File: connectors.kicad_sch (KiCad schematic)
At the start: 2 parts

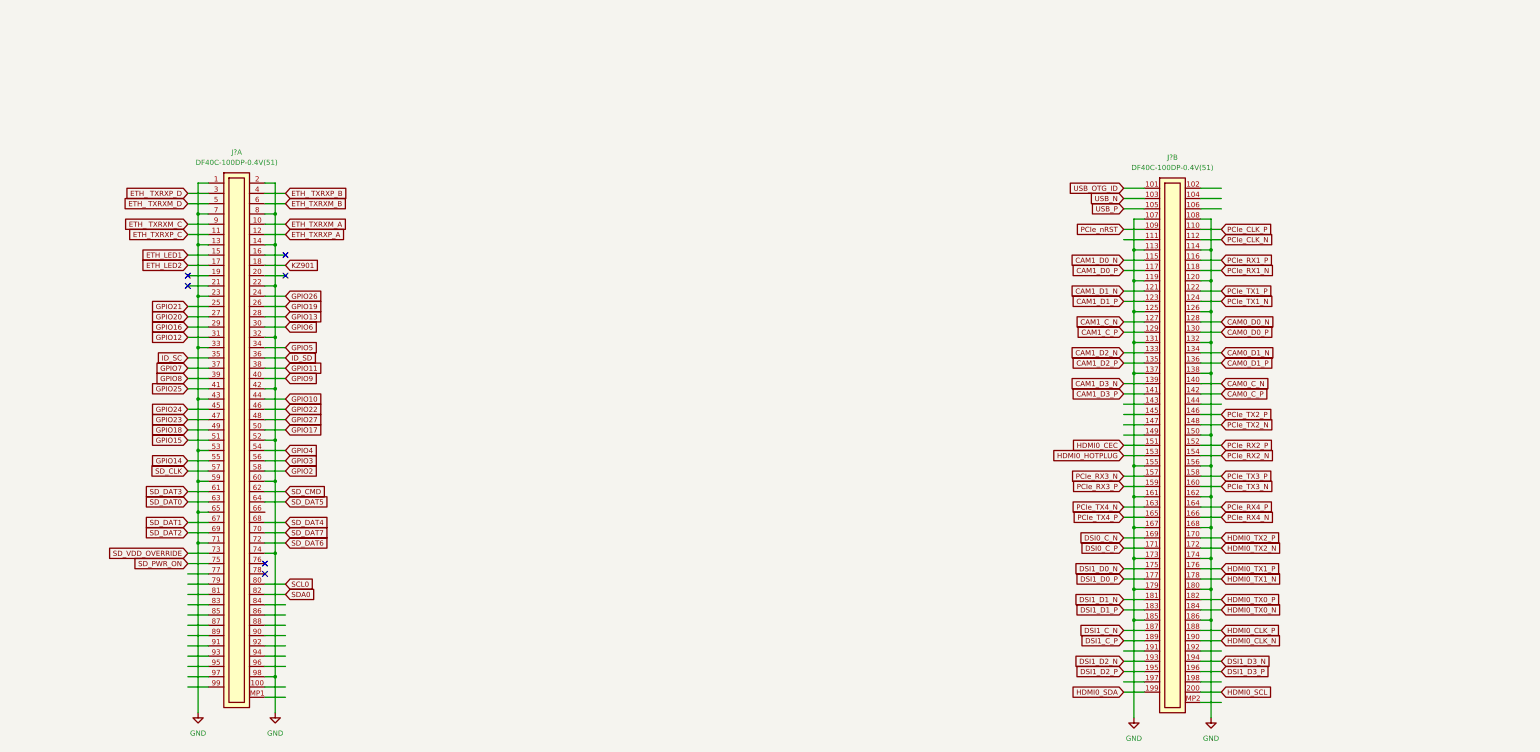
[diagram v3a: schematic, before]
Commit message: [#52579] Connect CSI and DSI to CrossLink
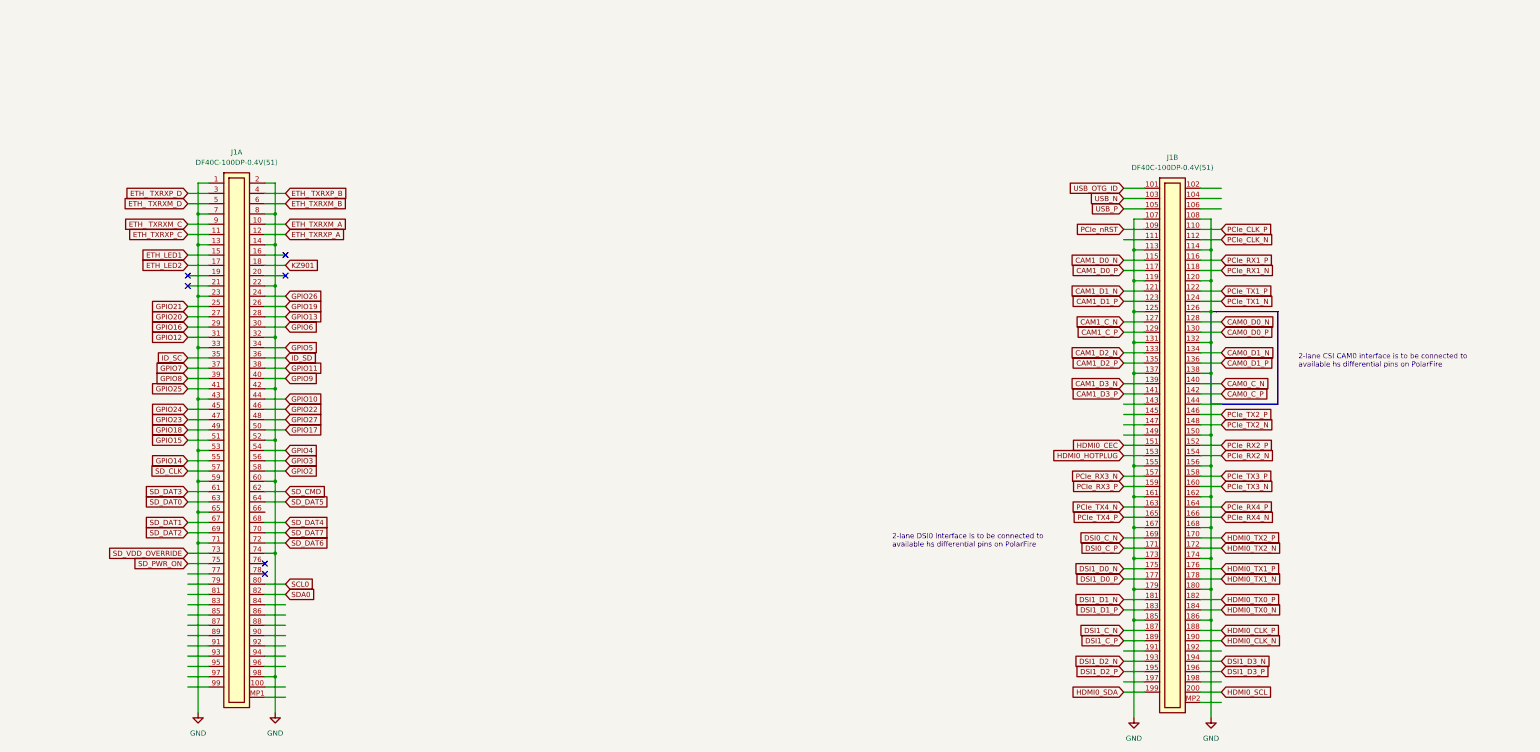
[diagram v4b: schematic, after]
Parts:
- gave numbers to parts that had none: 1
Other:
- note added: "2-lane CSI CAM0 interface is to be connected to available hs differential pins on PolarFire"
- note added: "2-lane DSI0 interface is to be connected to available hs differential pins on PolarFire"
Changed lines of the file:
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@@
+    (stroke (width 0) (type default) (color 0 0 0 0))
+  )
+  (polyline (pts (xy 328.93 111.76) (xy 344.17 111.76))
     (stroke (width 0) (type default) (color 0 0 0 0))
   )
@@
     (stroke (width 0) (type default) (color 0 0 0 0))
   )
+  (polyline (pts (xy 327.66 134.62) (xy 327.66 111.76))
+    (stroke (width 0) (type default) (color 0 0 0 0))
+  )
   (wire (pts (xy 306.07 106.68) (xy 311.15 106.68))
     (stroke (width 0) (type default) (color 0 0 0 0))
@@
     (stroke (width 0) (type default) (color 0 0 0 0))
   )
+  (polyline (pts (xy 344.17 111.76) (xy 344.17 134.62))
+    (stroke (width 0) (type default) (color 0 0 0 0))
+  )
   (wire (pts (xy 93.98 102.87) (xy 99.06 102.87))
     (stroke (width 0) (type default) (color 0 0 0 0))
@@
     (stroke (width 0) (type default) (color 0 0 0 0))
   )
+  (polyline (pts (xy 344.17 134.62) (xy 327.66 134.62))
+    (stroke (width 0) (type default) (color 0 0 0 0))
+  )
   (wire (pts (xy 74.93 176.53) (xy 80.01 176.53))
     (stroke (width 0) (type default) (color 0 0 0 0))
@@
     (stroke (width 0) (type default) (color 0 0 0 0))
   )
+  (polyline (pts (xy 327.66 111.76) (xy 328.93 111.76))
+    (stroke (width 0) (type default) (color 0 0 0 0))
+  )
   (wire (pts (xy 77.47 153.67) (xy 80.01 153.67))
     (stroke (width 0) (type default) (color 0 0 0 0))
@@
   (wire (pts (xy 74.93 85.09) (xy 80.01 85.09))
     (stroke (width 0) (type default) (color 0 0 0 0))
+  )
+  (text "2-lane CSI CAM0 interface is to be connected to \navailable hs differential pins on PolarFire"
+    (at 349.25 125.73 0)
+    (effects (font (size 1.27 1.27)) (justify left bottom))
+  )
+  (text "2-lane DSI0 interface is to be connected to \navailable hs differential pins on PolarFire"
+    (at 248.92 170.18 0)
+    (effects (font (size 1.27 1.27)) (justify left bottom))
   )
   (global_label "DSI1_C_N" (shape input) (at 306.07 190.5 180) (fields_autoplaced)
@@
   (symbol (lib_id "antmicropower:GND") (at 77.47 210.82 0) (unit 1)
     (in_bom yes) (on_board yes) (fields_autoplaced)
-    (property "Reference" "#PWR?" (id 0) (at 86.36 213.36 0)
+    (property "Reference" "#PWR01" (id 0) (at 86.36 213.36 0)
       (effects (font (size 1.27 1.27) (thickness 0.15)) (justify left bottom) hide)
     )
@@
   (symbol (lib_id "antmicroB2BConnectors:CM4_Plug_Module_Hirose_DF40_2x50_DF40C-100DP-0.4V_1") (at 311.15 81.28 0) (unit 2)
     (in_bom yes) (on_board yes) (fields_autoplaced)
-    (property "Reference" "J?" (id 0) (at 318.135 73.66 0)
+    (property "Reference" "J1" (id 0) (at 318.135 73.66 0)
       (effects (font (size 1.27 1.27) (thickness 0.15)))
     )
@@
   (symbol (lib_id "antmicroB2BConnectors:CM4_Plug_Module_Hirose_DF40_2x50_DF40C-100DP-0.4V_1") (at 80.01 80.01 0) (unit 1)
     (in_bom yes) (on_board yes) (fields_autoplaced)
-    (property "Reference" "J?" (id 0) (at 86.995 72.39 0)
+    (property "Reference" "J1" (id 0) (at 86.995 72.39 0)
       (effects (font (size 1.27 1.27) (thickness 0.15)))
     )
@@
   (symbol (lib_id "antmicropower:GND") (at 308.61 212.09 0) (unit 1)
     (in_bom yes) (on_board yes) (fields_autoplaced)
-    (property "Reference" "#PWR?" (id 0) (at 317.5 214.63 0)
+    (property "Reference" "#PWR03" (id 0) (at 317.5 214.63 0)
       (effects (font (size 1.27 1.27) (thickness 0.15)) (justify left bottom) hide)
     )
@@
   (symbol (lib_id "antmicropower:GND") (at 327.66 212.09 0) (unit 1)
     (in_bom yes) (on_board yes) (fields_autoplaced)
-    (property "Reference" "#PWR?" (id 0) (at 336.55 214.63 0)
+    (property "Reference" "#PWR04" (id 0) (at 336.55 214.63 0)
       (effects (font (size 1.27 1.27) (thickness 0.15)) (justify left bottom) hide)
     )
@@
   (symbol (lib_id "antmicropower:GND") (at 96.52 210.82 0) (unit 1)
     (in_bom yes) (on_board yes) (fields_autoplaced)
-    (property "Reference" "#PWR?" (id 0) (at 105.41 213.36 0)
-      (effects (font (size 1.27 1.27) (thickness 0.15)) (justify left bottom) hide)
-    )
+    (property "Reference" "#PWR02" (id 0) (at 105.41 213.36 0)
+      (effects (font (size 1.27 1.27) (thickness 0.15)) (justify left bottom) hide)
+    )

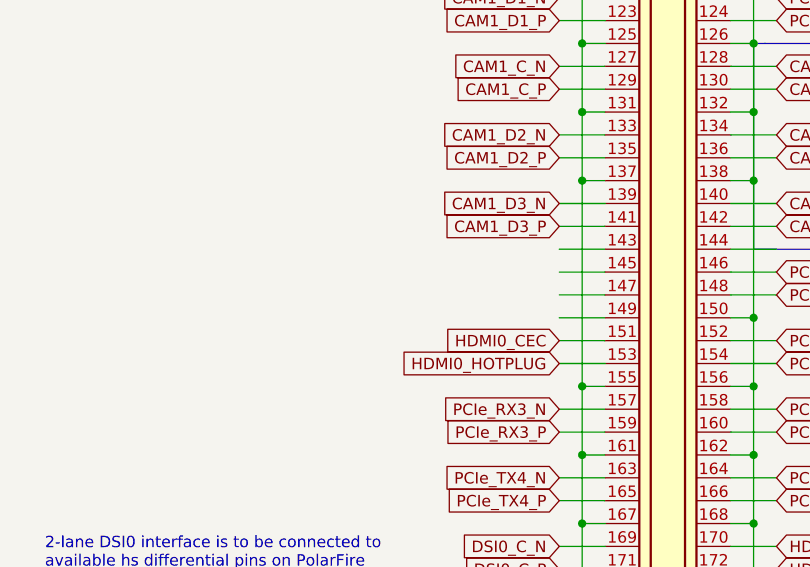
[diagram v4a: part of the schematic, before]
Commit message: [#53847] Add MIPI25 implementation of PF SoC
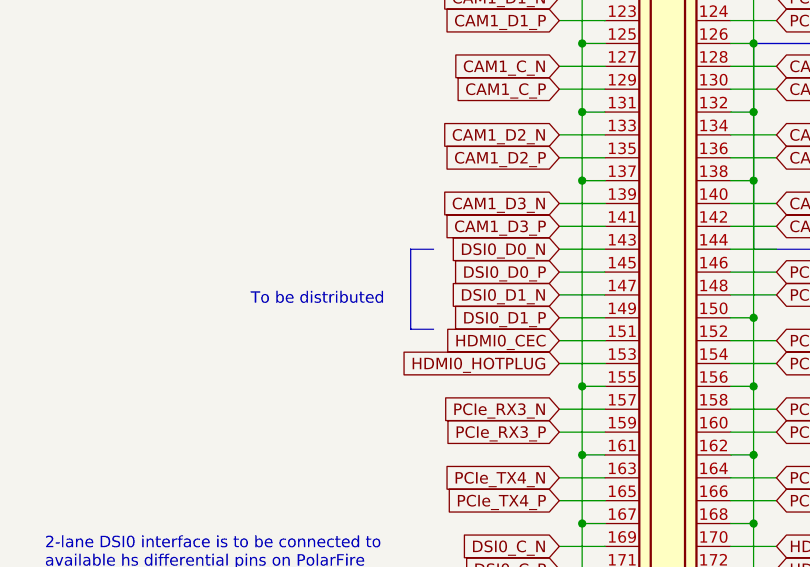
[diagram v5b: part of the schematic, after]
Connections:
- net DSI0_D0_N: now reaches J1.143
- net DSI0_D0_P: now reaches J1.145
- net DSI0_D1_N: now reaches J1.147
- net DSI0_D1_P: now reaches J1.149
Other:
- note added: "To be distributed"
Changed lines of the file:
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@@
+    (stroke (width 0) (type default) (color 0 0 0 0))
+  )
+  (polyline (pts (xy 289.56 134.62) (xy 289.56 143.51))
     (stroke (width 0) (type default) (color 0 0 0 0))
   )
@@
     (stroke (width 0) (type default) (color 0 0 0 0))
   )
+  (polyline (pts (xy 289.56 134.62) (xy 292.1 134.62))
+    (stroke (width 0) (type default) (color 0 0 0 0))
+  )
   (wire (pts (xy 325.12 203.2) (xy 330.2 203.2))
     (stroke (width 0) (type default) (color 0 0 0 0))
@@
   )
   (wire (pts (xy 74.93 110.49) (xy 80.01 110.49))
+    (stroke (width 0) (type default) (color 0 0 0 0))
+  )
+  (polyline (pts (xy 289.56 143.51) (xy 292.1 143.51))
     (stroke (width 0) (type default) (color 0 0 0 0))
   )
@@
     (effects (font (size 1.27 1.27)) (justify left bottom))
   )
+  (text "To be distributed" (at 271.78 140.97 0)
+    (effects (font (size 1.27 1.27)) (justify left bottom))
+  )
   (global_label "DSI1_C_N" (shape input) (at 306.07 190.5 180) (fields_autoplaced)
     (effects (font (size 1.27 1.27)) (justify right))
@@
     )
   )
+  (global_label "DSI0_D0_P" (shape input) (at 306.07 137.16 180) (fields_autoplaced)
+    (effects (font (size 1.27 1.27)) (justify right))
+    (property "Intersheet References" "${INTERSHEET_REFS}" (id 0) (at 293.6783 137.0806 0)
+      (effects (font (size 1.27 1.27)) (justify right) hide)
+    )
+  )
   (global_label "GPIO10" (shape input) (at 99.06 133.35 0) (fields_autoplaced)
     (effects (font (size 1.27 1.27)) (justify left))
@@
     )
   )
+  (global_label "DSI0_D1_N" (shape input) (at 306.07 139.7 180) (fields_autoplaced)
+    (effects (font (size 1.27 1.27)) (justify right))
+    (property "Intersheet References" "${INTERSHEET_REFS}" (id 0) (at 293.6179 139.6206 0)
+      (effects (font (size 1.27 1.27)) (justify right) hide)
+    )
+  )
   (global_label "CAM0_C_P" (shape input) (at 330.2 132.08 0) (fields_autoplaced)
     (effects (font (size 1.27 1.27)) (justify left))
@@
     )
   )
+  (global_label "DSI0_D1_P" (shape input) (at 306.07 142.24 180) (fields_autoplaced)
+    (effects (font (size 1.27 1.27)) (justify right))
+    (property "Intersheet References" "${INTERSHEET_REFS}" (id 0) (at 293.6783 142.1606 0)
+      (effects (font (size 1.27 1.27)) (justify right) hide)
+    )
+  )
   (global_label "GPIO19" (shape input) (at 99.06 110.49 0) (fields_autoplaced)
     (effects (font (size 1.27 1.27)) (justify left))
@@
       (effects (font (size 1.27 1.27)) (justify right) hide)
     )
+  )
+  (global_label "DSI0_D0_N" (shape input) (at 306.07 134.62 180) (fields_autoplaced)
+    (effects (font (size 1.27 1.27)) (justify right))
+    (property "Intersheet References" "${INTERSHEET_REFS}" (id 0) (at 293.6179 134.5406 0)
+      (effects (font (size 1.27 1.27)) (justify right) hide)
+    )

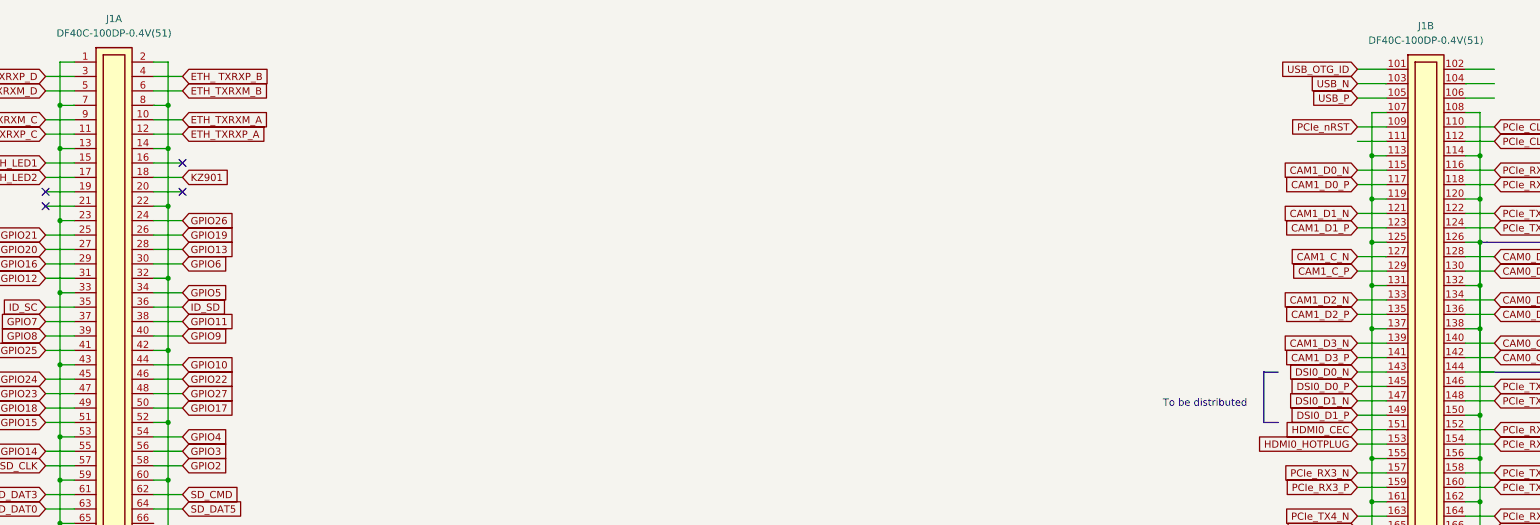
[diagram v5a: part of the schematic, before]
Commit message: [#52577] Clear annotations
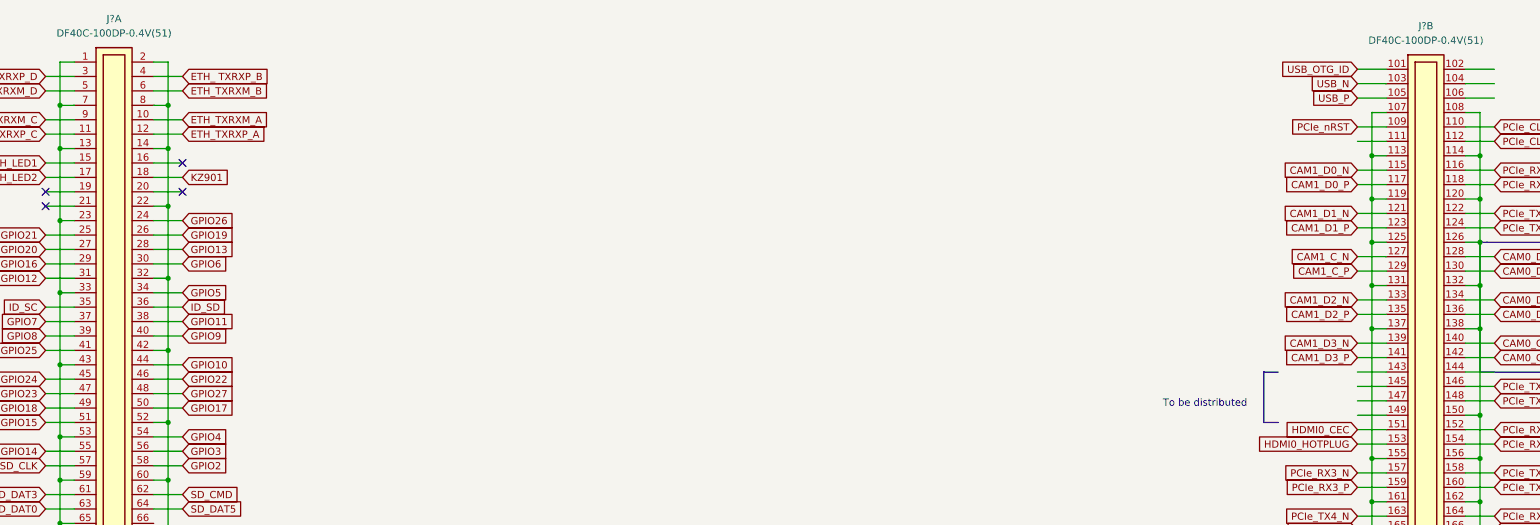
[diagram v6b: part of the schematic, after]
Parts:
- renumbered J1 to J?
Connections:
- net DSI0_D0_N: no longer names the net of J?.143
- net DSI0_D0_P: no longer names the net of J?.145
- net DSI0_D1_N: no longer names the net of J?.147
- net DSI0_D1_P: no longer names the net of J?.149
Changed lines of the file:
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@@
-    )
-  )
-  (global_label "DSI0_D0_P" (shape input) (at 306.07 137.16 180) (fields_autoplaced)
-    (effects (font (size 1.27 1.27)) (justify right))
-    (property "Intersheet References" "${INTERSHEET_REFS}" (id 0) (at 293.6783 137.0806 0)
-      (effects (font (size 1.27 1.27)) (justify right) hide)
     )
   )
@@
     )
   )
-  (global_label "DSI0_D1_N" (shape input) (at 306.07 139.7 180) (fields_autoplaced)
-    (effects (font (size 1.27 1.27)) (justify right))
-    (property "Intersheet References" "${INTERSHEET_REFS}" (id 0) (at 293.6179 139.6206 0)
-      (effects (font (size 1.27 1.27)) (justify right) hide)
-    )
-  )
   (global_label "CAM0_C_P" (shape input) (at 330.2 132.08 0) (fields_autoplaced)
     (effects (font (size 1.27 1.27)) (justify left))
@@
     )
   )
-  (global_label "DSI0_D1_P" (shape input) (at 306.07 142.24 180) (fields_autoplaced)
-    (effects (font (size 1.27 1.27)) (justify right))
-    (property "Intersheet References" "${INTERSHEET_REFS}" (id 0) (at 293.6783 142.1606 0)
-      (effects (font (size 1.27 1.27)) (justify right) hide)
-    )
-  )
   (global_label "GPIO19" (shape input) (at 99.06 110.49 0) (fields_autoplaced)
     (effects (font (size 1.27 1.27)) (justify left))
@@
     (effects (font (size 1.27 1.27)) (justify right))
     (property "Intersheet References" "${INTERSHEET_REFS}" (id 0) (at 294.8879 170.1006 0)
-      (effects (font (size 1.27 1.27)) (justify right) hide)
-    )
-  )
-  (global_label "DSI0_D0_N" (shape input) (at 306.07 134.62 180) (fields_autoplaced)
-    (effects (font (size 1.27 1.27)) (justify right))
-    (property "Intersheet References" "${INTERSHEET_REFS}" (id 0) (at 293.6179 134.5406 0)
       (effects (font (size 1.27 1.27)) (justify right) hide)
     )
@@
   (symbol (lib_id "antmicropower:GND") (at 77.47 210.82 0) (unit 1)
     (in_bom yes) (on_board yes) (fields_autoplaced)
-    (property "Reference" "#PWR01" (id 0) (at 86.36 213.36 0)
+    (property "Reference" "#PWR?" (id 0) (at 86.36 213.36 0)
       (effects (font (size 1.27 1.27) (thickness 0.15)) (justify left bottom) hide)
     )
@@
   (symbol (lib_id "antmicroB2BConnectors:CM4_Plug_Module_Hirose_DF40_2x50_DF40C-100DP-0.4V_1") (at 311.15 81.28 0) (unit 2)
     (in_bom yes) (on_board yes) (fields_autoplaced)
-    (property "Reference" "J1" (id 0) (at 318.135 73.66 0)
+    (property "Reference" "J?" (id 0) (at 318.135 73.66 0)
       (effects (font (size 1.27 1.27) (thickness 0.15)))
     )
@@
   (symbol (lib_id "antmicroB2BConnectors:CM4_Plug_Module_Hirose_DF40_2x50_DF40C-100DP-0.4V_1") (at 80.01 80.01 0) (unit 1)
     (in_bom yes) (on_board yes) (fields_autoplaced)
-    (property "Reference" "J1" (id 0) (at 86.995 72.39 0)
+    (property "Reference" "J?" (id 0) (at 86.995 72.39 0)
       (effects (font (size 1.27 1.27) (thickness 0.15)))
     )
@@
   (symbol (lib_id "antmicropower:GND") (at 308.61 212.09 0) (unit 1)
     (in_bom yes) (on_board yes) (fields_autoplaced)
-    (property "Reference" "#PWR03" (id 0) (at 317.5 214.63 0)
+    (property "Reference" "#PWR?" (id 0) (at 317.5 214.63 0)
       (effects (font (size 1.27 1.27) (thickness 0.15)) (justify left bottom) hide)
     )
@@
   (symbol (lib_id "antmicropower:GND") (at 327.66 212.09 0) (unit 1)
     (in_bom yes) (on_board yes) (fields_autoplaced)
-    (property "Reference" "#PWR04" (id 0) (at 336.55 214.63 0)
+    (property "Reference" "#PWR?" (id 0) (at 336.55 214.63 0)
       (effects (font (size 1.27 1.27) (thickness 0.15)) (justify left bottom) hide)
     )
@@
   (symbol (lib_id "antmicropower:GND") (at 96.52 210.82 0) (unit 1)
     (in_bom yes) (on_board yes) (fields_autoplaced)
-    (property "Reference" "#PWR02" (id 0) (at 105.41 213.36 0)
-      (effects (font (size 1.27 1.27) (thickness 0.15)) (justify left bottom) hide)
-    )
+    (property "Reference" "#PWR?" (id 0) (at 105.41 213.36 0)
+      (effects (font (size 1.27 1.27) (thickness 0.15)) (justify left bottom) hide)
+    )
